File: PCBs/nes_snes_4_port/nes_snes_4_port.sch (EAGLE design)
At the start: 40 parts, among them J5 RJ45, J6 RJ45, J7 RJ45, J8 RJ45, J9 RJ45-S-4, U1 74245, U10 MC74VHC1GT125, U2 MC74VHC1GT125, U3 MC74VHC1GT125, U4 MC74VHC1GT125, U5 MC74VHC1GT125, U7 MC74VHC1GT125, U8 MC74VHC1GT125, U9 MC74VHC1GT125

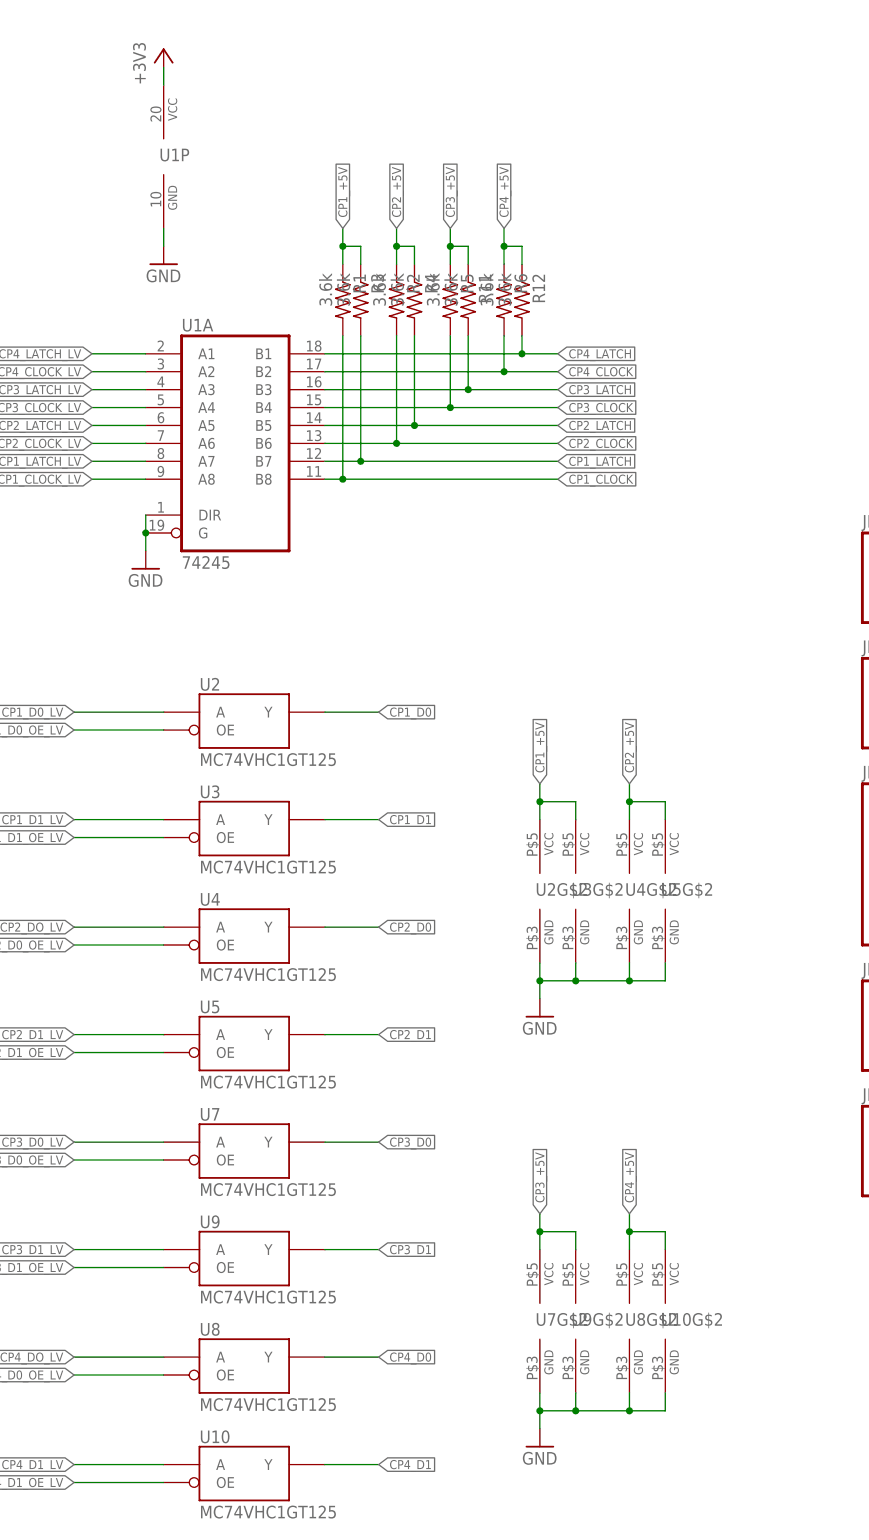
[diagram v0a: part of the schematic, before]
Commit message: 4 port PCB: Added decoupling capacitors.
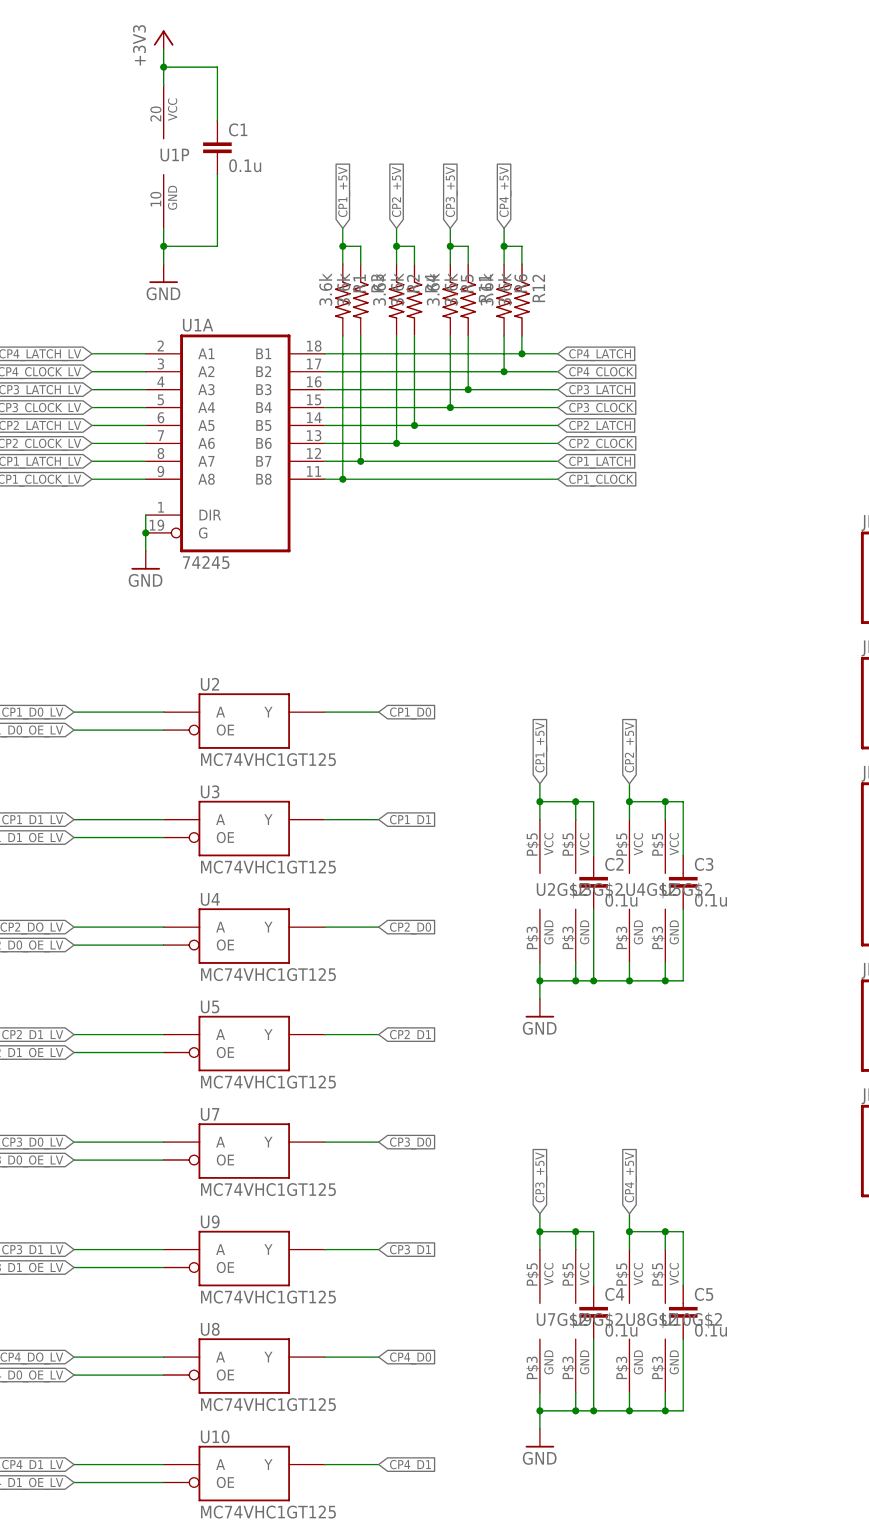
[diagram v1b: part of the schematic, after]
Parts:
- added C1, C2, C3, C4, C5: 0.1u, rcl:C-EUC0603
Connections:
- net +3V3: now also C1.1
- net CP1_+5V: now also C2.1
- net CP2_+5V: now also C3.1
- net CP3_+5V: now also C4.1
- net CP4_+5V: now also C5.1
- net GND: now also C1.2, C2.2, C3.2, C4.2, C5.2
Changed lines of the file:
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@@
 <part name="JP6" library="SparkFun-Connectors" deviceset="M08" device="1X08"/>
 <part name="JP9" library="SparkFun-Connectors" deviceset="M08" device="1X08"/>
+<part name="C1" library="rcl" deviceset="C-EU" device="C0603" value="0.1u"/>
+<part name="C2" library="rcl" deviceset="C-EU" device="C0603" value="0.1u"/>
+<part name="C3" library="rcl" deviceset="C-EU" device="C0603" value="0.1u"/>
+<part name="C4" library="rcl" deviceset="C-EU" device="C0603" value="0.1u"/>
+<part name="C5" library="rcl" deviceset="C-EU" device="C0603" value="0.1u"/>
 </parts>
 <sheets>
@@
 <instance part="GND3" gate="1" x="-129.54" y="-99.06"/>
 <instance part="GND4" gate="1" x="-78.74" y="12.7"/>
-<instance part="+3V2" gate="G$1" x="-76.2" y="86.36"/>
-<instance part="GND5" gate="1" x="-76.2" y="55.88"/>
+<instance part="+3V2" gate="G$1" x="-76.2" y="88.9"/>
+<instance part="GND5" gate="1" x="-76.2" y="53.34"/>
 <instance part="R1" gate="G$1" x="-50.8" y="50.8" rot="R270"/>
 <instance part="R2" gate="G$1" x="-43.18" y="50.8" rot="R270"/>
@@
 <instance part="JP6" gate="G$1" x="322.58" y="2.54" rot="MR180"/>
 <instance part="JP9" gate="G$1" x="414.02" y="-78.74" rot="MR180"/>
+<instance part="C1" gate="G$1" x="-68.58" y="73.66"/>
+<instance part="C2" gate="G$1" x="-15.24" y="-30.48"/>
+<instance part="C3" gate="G$1" x="-2.54" y="-30.48"/>
+<instance part="C4" gate="G$1" x="-15.24" y="-91.44"/>
+<instance part="C5" gate="G$1" x="-2.54" y="-91.44"/>
 </instances>
 <busses>
@@
 <pinref part="U1" gate="P" pin="VCC"/>
 <pinref part="+3V2" gate="G$1" pin="+3V3"/>
+<wire x1="-76.2" y1="86.36" x2="-76.2" y2="83.82" width="0.1524" layer="91"/>
+<pinref part="C1" gate="G$1" pin="1"/>
 <wire x1="-76.2" y1="83.82" x2="-76.2" y2="81.28" width="0.1524" layer="91"/>
+<wire x1="-76.2" y1="83.82" x2="-68.58" y2="83.82" width="0.1524" layer="91"/>
+<wire x1="-68.58" y1="83.82" x2="-68.58" y2="76.2" width="0.1524" layer="91"/>
+<junction x="-76.2" y="83.82"/>
 </segment>
 <segment>
@@
 <pinref part="U1" gate="P" pin="GND"/>
 <pinref part="GND5" gate="1" pin="GND"/>
+<wire x1="-76.2" y1="55.88" x2="-76.2" y2="58.42" width="0.1524" layer="91"/>
+<pinref part="C1" gate="G$1" pin="2"/>
 <wire x1="-76.2" y1="58.42" x2="-76.2" y2="60.96" width="0.1524" layer="91"/>
+<wire x1="-76.2" y1="58.42" x2="-68.58" y2="58.42" width="0.1524" layer="91"/>
+<wire x1="-68.58" y1="58.42" x2="-68.58" y2="68.58" width="0.1524" layer="91"/>
+<junction x="-76.2" y="58.42"/>
 </segment>
 <segment>
@@
 <wire x1="-10.16" y1="-45.72" x2="-10.16" y2="-43.18" width="0.1524" layer="91"/>
 <wire x1="-5.08" y1="-45.72" x2="-10.16" y2="-45.72" width="0.1524" layer="91"/>
-<wire x1="-10.16" y1="-45.72" x2="-17.78" y2="-45.72" width="0.1524" layer="91"/>
+<wire x1="-10.16" y1="-45.72" x2="-15.24" y2="-45.72" width="0.1524" layer="91"/>
 <junction x="-10.16" y="-45.72"/>
 <junction x="-17.78" y="-45.72"/>
 <junction x="-22.86" y="-45.72"/>
+<pinref part="C2" gate="G$1" pin="2"/>
+<wire x1="-15.24" y1="-45.72" x2="-17.78" y2="-45.72" width="0.1524" layer="91"/>
+<wire x1="-15.24" y1="-35.56" x2="-15.24" y2="-45.72" width="0.1524" layer="91"/>
+<pinref part="C3" gate="G$1" pin="2"/>
+<wire x1="-5.08" y1="-45.72" x2="-2.54" y2="-45.72" width="0.1524" layer="91"/>
+<wire x1="-2.54" y1="-45.72" x2="-2.54" y2="-35.56" width="0.1524" layer="91"/>
+<junction x="-15.24" y="-45.72"/>
+<junction x="-5.08" y="-45.72"/>
 </segment>
 <segment>
@@
 <wire x1="-10.16" y1="-106.68" x2="-10.16" y2="-104.14" width="0.1524" layer="91"/>
 <wire x1="-5.08" y1="-106.68" x2="-10.16" y2="-106.68" width="0.1524" layer="91"/>
-<wire x1="-10.16" y1="-106.68" x2="-17.78" y2="-106.68" width="0.1524" layer="91"/>
+<wire x1="-10.16" y1="-106.68" x2="-15.24" y2="-106.68" width="0.1524" layer="91"/>
 <junction x="-10.16" y="-106.68"/>
 <junction x="-17.78" y="-106.68"/>
 <junction x="-22.86" y="-106.68"/>
+<pinref part="C4" gate="G$1" pin="2"/>
+<wire x1="-15.24" y1="-106.68" x2="-17.78" y2="-106.68" width="0.1524" layer="91"/>
+<wire x1="-15.24" y1="-96.52" x2="-15.24" y2="-106.68" width="0.1524" layer="91"/>
+<pinref part="C5" gate="G$1" pin="2"/>
+<wire x1="-5.08" y1="-106.68" x2="-2.54" y2="-106.68" width="0.1524" layer="91"/>
+<wire x1="-2.54" y1="-106.68" x2="-2.54" y2="-96.52" width="0.1524" layer="91"/>
+<junction x="-5.08" y="-106.68"/>
+<junction x="-15.24" y="-106.68"/>
 </segment>
 <segment>
@@
 <junction x="-22.86" y="-20.32"/>
 <label x="-22.86" y="-17.78" size="1.27" layer="95" rot="R90" xref="yes"/>
+<pinref part="C2" gate="G$1" pin="1"/>
+<wire x1="-17.78" y1="-20.32" x2="-15.24" y2="-20.32" width="0.1524" layer="91"/>
+<wire x1="-15.24" y1="-20.32" x2="-15.24" y2="-27.94" width="0.1524" layer="91"/>
+<junction x="-17.78" y="-20.32"/>
 </segment>
 </net>
@@
 <junction x="-10.16" y="-20.32"/>
 <label x="-10.16" y="-17.78" size="1.27" layer="95" rot="R90" xref="yes"/>
+<pinref part="C3" gate="G$1" pin="1"/>
+<wire x1="-5.08" y1="-20.32" x2="-2.54" y2="-20.32" width="0.1524" layer="91"/>
+<wire x1="-2.54" y1="-20.32" x2="-2.54" y2="-27.94" width="0.1524" layer="91"/>
+<junction x="-5.08" y="-20.32"/>
 </segment>
 <segment>
@@
 <junction x="-22.86" y="-81.28"/>
 <label x="-22.86" y="-78.74" size="1.27" layer="95" rot="R90" xref="yes"/>
+<pinref part="C4" gate="G$1" pin="1"/>
+<wire x1="-17.78" y1="-81.28" x2="-15.24" y2="-81.28" width="0.1524" layer="91"/>
+<wire x1="-15.24" y1="-81.28" x2="-15.24" y2="-88.9" width="0.1524" layer="91"/>
+<junction x="-17.78" y="-81.28"/>
 </segment>
 <segment>
@@
 <junction x="-10.16" y="-81.28"/>
 <label x="-10.16" y="-78.74" size="1.27" layer="95" rot="R90" xref="yes"/>
-</segment>
-<segment>
+<pinref part="C5" gate="G$1" pin="1"/>
+<wire x1="-5.08" y1="-81.28" x2="-2.54" y2="-81.28" width="0.1524" layer="91"/>
+<wire x1="-2.54" y1="-81.28" x2="-2.54" y2="-88.9" width="0.1524" layer="91"/>
+<junction x="-5.08" y="-81.28"/>
+</segment>
+<segment>

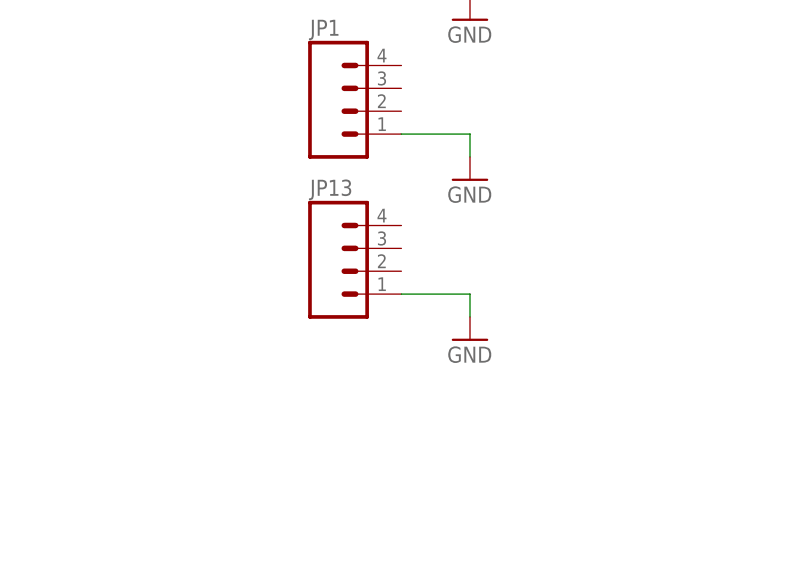
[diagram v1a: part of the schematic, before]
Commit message: NES/SNES 4-port PCB: Removed the power supply pins that did nothing. Fixed the backwards power supply pin. Added 4 ground tap pins.
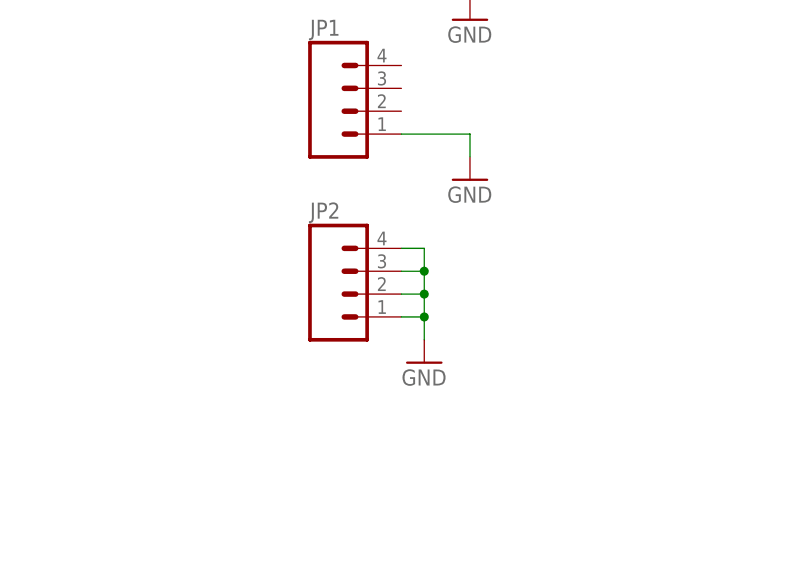
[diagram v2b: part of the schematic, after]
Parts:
- removed JP13: (no value), SparkFun-Connectors:M04PTH
- added JP2: (no value), SparkFun-Connectors:M04PTH
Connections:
- net GND: now also JP2.1, JP2.2, JP2.3, JP2.4; no longer JP13.1
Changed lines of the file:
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@@
 <part name="JP1" library="SparkFun-Connectors" deviceset="M04" device="PTH"/>
 <part name="GND1" library="supply1" deviceset="GND" device=""/>
-<part name="JP13" library="SparkFun-Connectors" deviceset="M04" device="PTH"/>
-<part name="GND15" library="supply1" deviceset="GND" device=""/>
 <part name="JP14" library="SparkFun-Connectors" deviceset="M08" device="1X08"/>
 <part name="JP15" library="SparkFun-Connectors" deviceset="M04" device="PTH"/>
@@
 <part name="C4" library="rcl" deviceset="C-EU" device="C0603" value="0.1u"/>
 <part name="C5" library="rcl" deviceset="C-EU" device="C0603" value="0.1u"/>
+<part name="JP2" library="SparkFun-Connectors" deviceset="M04" device="PTH"/>
+<part name="GND15" library="supply1" deviceset="GND" device=""/>
 </parts>
 <sheets>
@@
 <instance part="JP1" gate="G$1" x="322.58" y="-50.8"/>
 <instance part="GND1" gate="1" x="335.28" y="-58.42"/>
-<instance part="JP13" gate="G$1" x="322.58" y="-68.58"/>
-<instance part="GND15" gate="1" x="335.28" y="-76.2"/>
 <instance part="JP14" gate="G$1" x="414.02" y="-17.78"/>
 <instance part="JP15" gate="G$1" x="414.02" y="-40.64"/>
@@
 <instance part="C4" gate="G$1" x="-15.24" y="-91.44"/>
 <instance part="C5" gate="G$1" x="-2.54" y="-91.44"/>
+<instance part="JP2" gate="G$1" x="322.58" y="-71.12"/>
+<instance part="GND15" gate="1" x="330.2" y="-78.74"/>
 </instances>
 <busses>
@@
 </segment>
 <segment>
-<pinref part="JP13" gate="G$1" pin="1"/>
-<pinref part="GND15" gate="1" pin="GND"/>
-<wire x1="327.66" y1="-71.12" x2="335.28" y2="-71.12" width="0.1524" layer="91"/>
-<wire x1="335.28" y1="-71.12" x2="335.28" y2="-73.66" width="0.1524" layer="91"/>
-</segment>
-<segment>
 <wire x1="419.1" y1="5.08" x2="434.34" y2="5.08" width="0.1524" layer="91"/>
 <wire x1="434.34" y1="5.08" x2="434.34" y2="2.54" width="0.1524" layer="91"/>
@@
 <pinref part="JP21" gate="G$1" pin="1"/>
 </segment>
+<segment>
+<pinref part="JP2" gate="G$1" pin="4"/>
+<pinref part="GND15" gate="1" pin="GND"/>
+<wire x1="327.66" y1="-66.04" x2="330.2" y2="-66.04" width="0.1524" layer="91"/>
+<wire x1="330.2" y1="-66.04" x2="330.2" y2="-68.58" width="0.1524" layer="91"/>
+<pinref part="JP2" gate="G$1" pin="3"/>
+<wire x1="330.2" y1="-68.58" x2="330.2" y2="-71.12" width="0.1524" layer="91"/>
+<wire x1="330.2" y1="-71.12" x2="330.2" y2="-73.66" width="0.1524" layer="91"/>
+<wire x1="330.2" y1="-73.66" x2="330.2" y2="-76.2" width="0.1524" layer="91"/>
+<wire x1="327.66" y1="-68.58" x2="330.2" y2="-68.58" width="0.1524" layer="91"/>
+<pinref part="JP2" gate="G$1" pin="2"/>
+<wire x1="327.66" y1="-71.12" x2="330.2" y2="-71.12" width="0.1524" layer="91"/>
+<pinref part="JP2" gate="G$1" pin="1"/>
+<wire x1="327.66" y1="-73.66" x2="330.2" y2="-73.66" width="0.1524" layer="91"/>
+<junction x="330.2" y="-68.58"/>
+<junction x="330.2" y="-71.12"/>
+<junction x="330.2" y="-73.66"/>
+</segment>
 </net>
